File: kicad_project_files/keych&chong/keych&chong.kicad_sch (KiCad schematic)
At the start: 229 parts, among them J1 USB_C_Receptacle_USB2.0, U1 ATmega32U4-A, Y1 Crystal

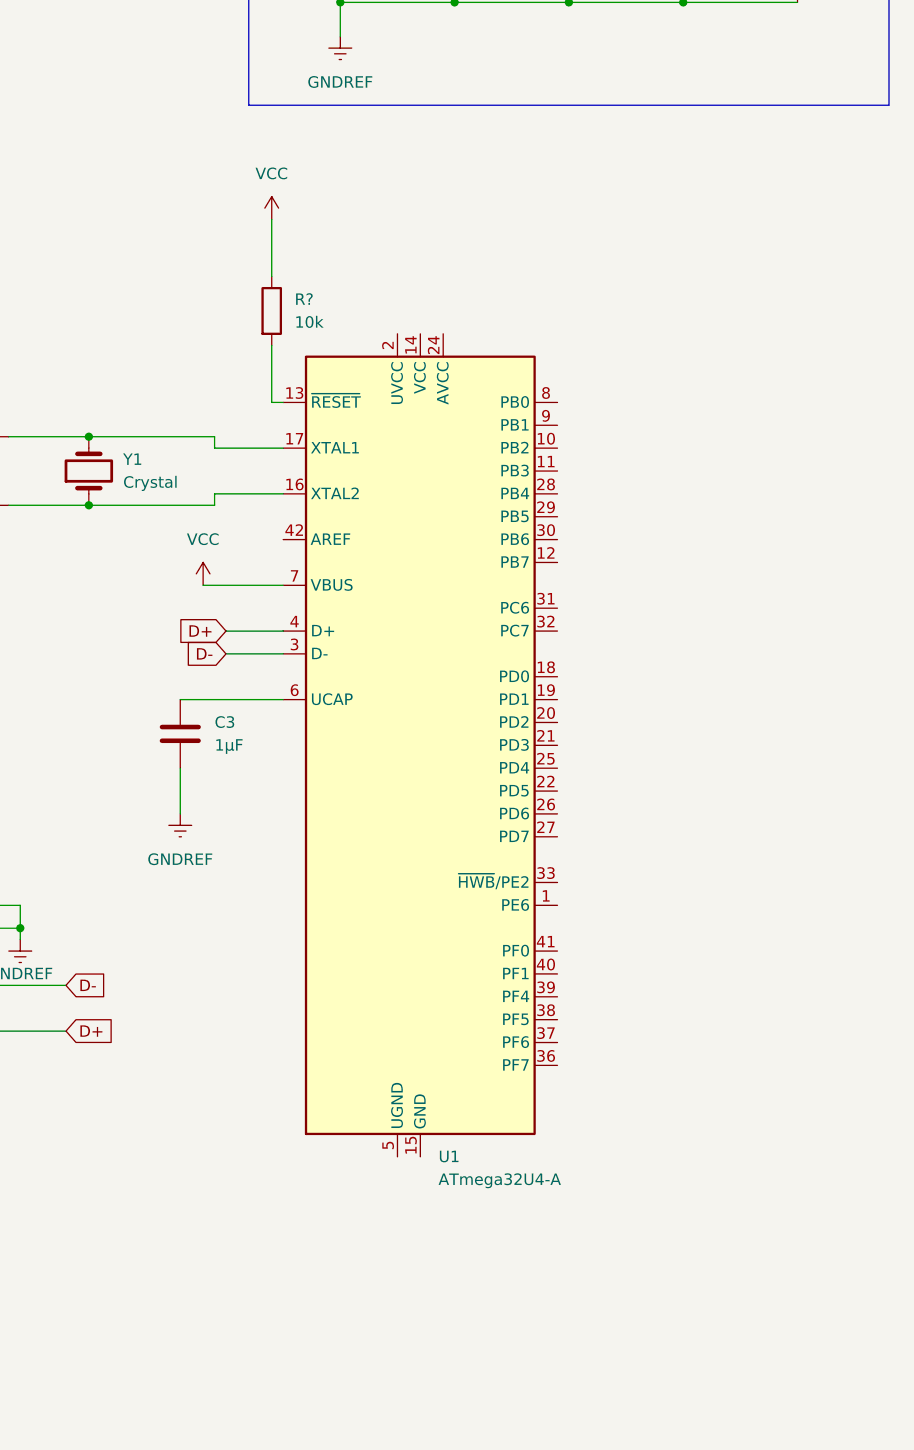
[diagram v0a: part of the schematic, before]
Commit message: refactor folder structure and add test circuit
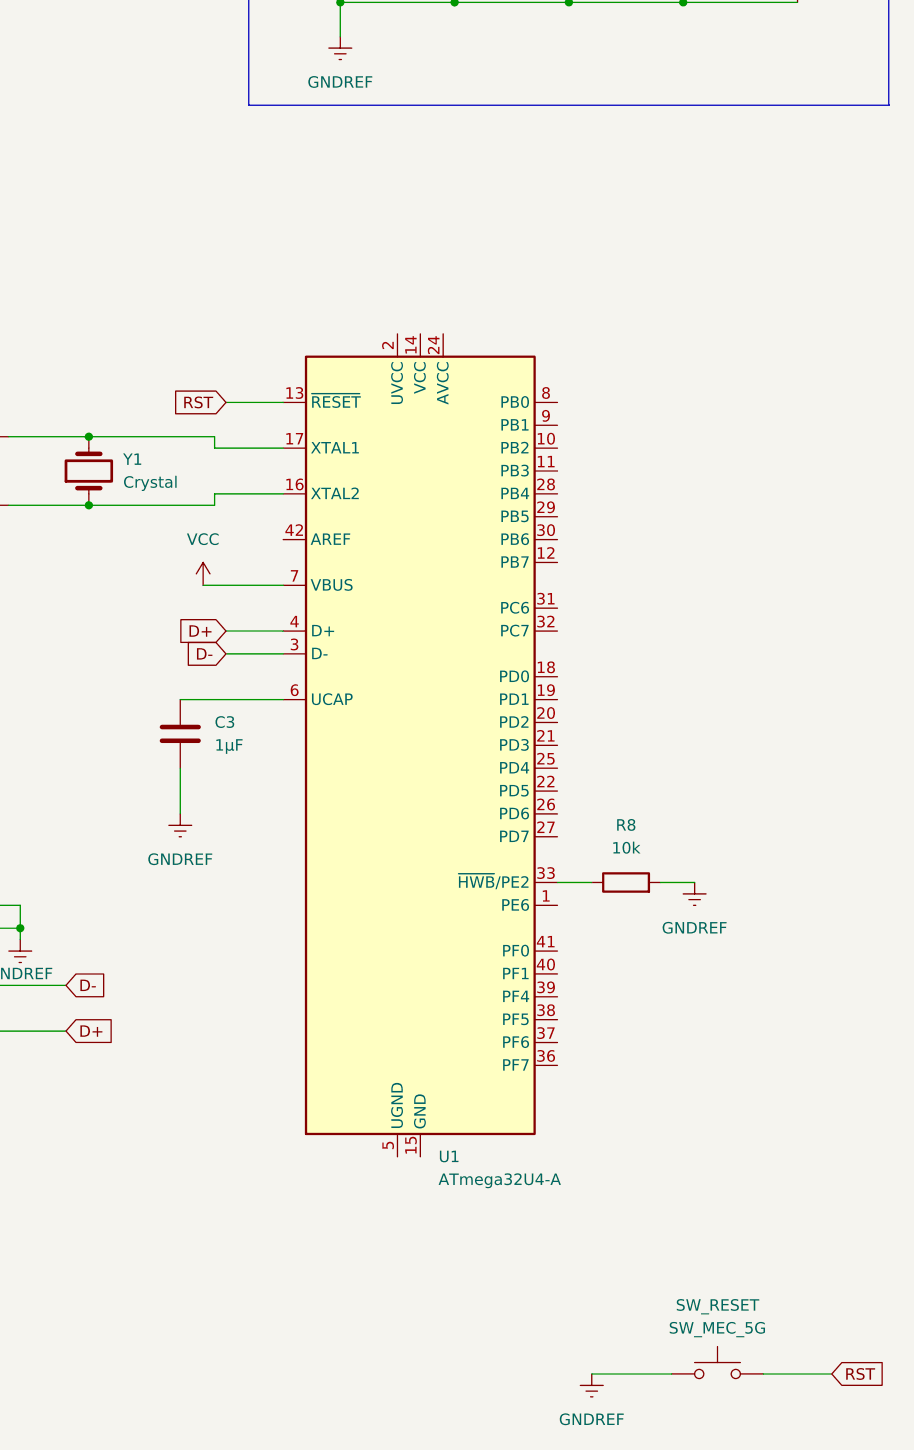
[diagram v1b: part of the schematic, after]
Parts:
- removed R?: 10k, symbol Device:R
- added R8: 10k, symbol Device:R
- added SW_RESET: SW_MEC_5G, symbol Switch:SW_MEC_5G
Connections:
- net GNDREF: now also R8.2, SW_RESET.1 (A), SW_RESET.2 (A)
- net RST: now reaches U1.13 (~{RESET})
- net RST: now also SW_RESET.3 (B), SW_RESET.4 (B)
- net at U1.33 (~{HWB}/PE2): now also R8.1
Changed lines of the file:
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@@
     (stroke (width 0) (type default) (color 0 0 0 0))
   )
-  (wire (pts (xy 326.39 132.08) (xy 326.39 125.73))
-    (stroke (width 0) (type default) (color 0 0 0 0))
-  )
   (wire (pts (xy 228.6 73.66) (xy 243.84 73.66))
     (stroke (width 0) (type default) (color 0 0 0 0))
@@
     (stroke (width 0) (type default) (color 0 0 0 0))
   )
+  (wire (pts (xy 381 240.03) (xy 388.62 240.03))
+    (stroke (width 0) (type default) (color 0 0 0 0))
+  )
   (wire (pts (xy 147.32 129.54) (xy 147.32 151.13))
     (stroke (width 0) (type default) (color 0 0 0 0))
@@
     (stroke (width 0) (type default) (color 0 0 0 0))
   )
+  (wire (pts (xy 369.57 185.42) (xy 373.38 185.42))
+    (stroke (width 0) (type default) (color 0 0 0 0))
+  )
   (wire (pts (xy 137.16 116.84) (xy 152.4 116.84))
     (stroke (width 0) (type default) (color 0 0 0 0))
@@
     (stroke (width 0) (type default) (color 0 0 0 0))
   )
-  (wire (pts (xy 327.66 132.08) (xy 326.39 132.08))
+  (wire (pts (xy 321.31 132.08) (xy 327.66 132.08))
     (stroke (width 0) (type default) (color 0 0 0 0))
   )
@@
     (stroke (width 0) (type default) (color 0 0 0 0))
   )
+  (wire (pts (xy 358.14 185.42) (xy 361.95 185.42))
+    (stroke (width 0) (type default) (color 0 0 0 0))
+  )
   (wire (pts (xy 106.68 106.68) (xy 106.68 109.22))
     (stroke (width 0) (type default) (color 0 0 0 0))
@@
     (stroke (width 0) (type default) (color 0 0 0 0))
   )
+  (wire (pts (xy 361.95 240.03) (xy 370.84 240.03))
+    (stroke (width 0) (type default) (color 0 0 0 0))
+  )
   (wire (pts (xy 76.2 161.29) (xy 91.44 161.29))
     (stroke (width 0) (type default) (color 0 0 0 0))
@@
     (stroke (width 0) (type default) (color 0 0 0 0))
   )
-  (wire (pts (xy 326.39 111.76) (xy 326.39 118.11))
-    (stroke (width 0) (type default) (color 0 0 0 0))
-  )
   (polyline (pts (xy 337.82 64.77) (xy 394.97 64.77))
     (stroke (width 0) (type default) (color 0 0 0 0))
@@
     )
   )
+  (global_label "RST" (shape input) (at 388.62 240.03 0) (fields_autoplaced)
+    (effects (font (size 1.27 1.27)) (justify left))
+    (property "Intersheet References" "${INTERSHEET_REFS}" (id 0) (at 394.4802 239.9506 0)
+      (effects (font (size 1.27 1.27)) (justify left) hide)
+    )
+  )
   (global_label "ROW_5" (shape input) (at 22.86 140.97 180) (fields_autoplaced)
     (effects (font (size 1.27 1.27)) (justify right))
@@
     )
   )
+  (global_label "RST" (shape input) (at 321.31 132.08 180) (fields_autoplaced)
+    (effects (font (size 1.27 1.27)) (justify right))
+    (property "Intersheet References" "${INTERSHEET_REFS}" (id 0) (at 315.4498 132.0006 0)
+      (effects (font (size 1.27 1.27)) (justify right) hide)
+    )
+  )
   (global_label "ROW_6" (shape input) (at 22.86 163.83 180) (fields_autoplaced)
     (effects (font (size 1.27 1.27)) (justify right))
@@
     (pin "4")
   )
+  (symbol (lib_id "Device:R") (at 365.76 185.42 90) (unit 1)
+    (in_bom yes) (on_board yes) (fields_autoplaced)
+    (property "Reference" "R8" (id 0) (at 365.76 179.07 90))
+    (property "Value" "10k" (id 1) (at 365.76 181.61 90))
+    (property "Footprint" "" (id 2) (at 365.76 187.198 90)
+      (effects (font (size 1.27 1.27)) hide)
+    )
+    (property "Datasheet" "~" (id 3) (at 365.76 185.42 0)
+      (effects (font (size 1.27 1.27)) hide)
+    )
+    (pin "1")
+    (pin "2")
+  )
   (symbol (lib_id "Switch:SW_MEC_5G") (at 264.16 41.91 0) (unit 1)
     (in_bom yes) (on_board yes) (fields_autoplaced)
@@
     (pin "4")
   )
-  (symbol (lib_id "power:VCC") (at 326.39 111.76 0) (unit 1)
-    (in_bom yes) (on_board yes) (fields_autoplaced)
-    (property "Reference" "#PWR?" (id 0) (at 326.39 115.57 0)
-      (effects (font (size 1.27 1.27)) hide)
-    )
-    (property "Value" "VCC" (id 1) (at 326.39 106.68 0))
-    (property "Footprint" "" (id 2) (at 326.39 111.76 0)
-      (effects (font (size 1.27 1.27)) hide)
-    )
-    (property "Datasheet" "" (id 3) (at 326.39 111.76 0)
-      (effects (font (size 1.27 1.27)) hide)
-    )
-    (pin "1")
-  )
   (symbol (lib_id "Diode:1N4148") (at 91.44 69.85 90) (unit 1)
     (in_bom yes) (on_board yes) (fields_autoplaced)
@@
     (pin "4")
   )
+  (symbol (lib_id "power:GNDREF") (at 373.38 185.42 0) (unit 1)
+    (in_bom yes) (on_board yes) (fields_autoplaced)
+    (property "Reference" "#PWR013" (id 0) (at 373.38 191.77 0)
+      (effects (font (size 1.27 1.27)) hide)
+    )
+    (property "Value" "GNDREF" (id 1) (at 373.38 190.5 0))
+    (property "Footprint" "" (id 2) (at 373.38 185.42 0)
+      (effects (font (size 1.27 1.27)) hide)
+    )
+    (property "Datasheet" "" (id 3) (at 373.38 185.42 0)
+      (effects (font (size 1.27 1.27)) hide)
+    )
+    (pin "1")
+  )
   (symbol (lib_id "power:VCC") (at 334.01 76.2 0) (unit 1)
     (in_bom yes) (on_board yes) (fields_autoplaced)
@@
     (pin "4")
   )
-  (symbol (lib_id "Device:R") (at 326.39 121.92 0) (unit 1)
-    (in_bom yes) (on_board yes) (fields_autoplaced)
-    (property "Reference" "R?" (id 0) (at 328.93 120.6499 0)
-      (effects (font (size 1.27 1.27)) (justify left))
-    )
-    (property "Value" "10k" (id 1) (at 328.93 123.1899 0)
-      (effects (font (size 1.27 1.27)) (justify left))
-    )
-    (property "Footprint" "" (id 2) (at 324.612 121.92 90)
-      (effects (font (size 1.27 1.27)) hide)
-    )
-    (property "Datasheet" "~" (id 3) (at 326.39 121.92 0)
-      (effects (font (size 1.27 1.27)) hide)
-    )
-    (pin "1")
-    (pin "2")
-  )
   (symbol (lib_id "Diode:1N4148") (at 152.4 69.85 90) (unit 1)
     (in_bom yes) (on_board yes) (fields_autoplaced)
@@
     (pin "4")
   )
+  (symbol (lib_id "power:GNDREF") (at 361.95 240.03 0) (unit 1)
+    (in_bom yes) (on_board yes) (fields_autoplaced)
+    (property "Reference" "#PWR012" (id 0) (at 361.95 246.38 0)
+      (effects (font (size 1.27 1.27)) hide)
+    )
+    (property "Value" "GNDREF" (id 1) (at 361.95 245.11 0))
+    (property "Footprint" "" (id 2) (at 361.95 240.03 0)
+      (effects (font (size 1.27 1.27)) hide)
+    )
+    (property "Datasheet" "" (id 3) (at 361.95 240.03 0)
+      (effects (font (size 1.27 1.27)) hide)
+    )
+    (pin "1")
+  )
   (symbol (lib_id "Diode:1N4148") (at 45.72 157.48 90) (unit 1)
     (in_bom yes) (on_board yes) (fields_autoplaced)
@@
     (pin "2")
   )
+  (symbol (lib_id "Switch:SW_MEC_5G") (at 375.92 240.03 0) (unit 1)
+    (in_bom yes) (on_board yes) (fields_autoplaced)
+    (property "Reference" "SW_RESET" (id 0) (at 375.92 232.41 0))
+    (property "Value" "SW_MEC_5G" (id 1) (at 375.92 234.95 0))
+    (property "Footprint" "" (id 2) (at 375.92 234.95 0)
+      (effects (font (size 1.27 1.27)) hide)
+    )
+    (property "Datasheet" "http://www.apem.com/int/index.php?controller=attachment&id_attachment=488" (id 3) (at 375.92 234.95 0)
+      (effects (font (size 1.27 1.27)) hide)
+    )
+    (pin "1")
+    (pin "3")
+    (pin "2")
+    (pin "4")
+  )
   (symbol (lib_id "Diode:1N4148") (at 45.72 113.03 90) (unit 1)
     (in_bom yes) (on_board yes) (fields_autoplaced)
@@
       (reference "#PWR011") (unit 1) (value "VCC") (footprint "")
     )
-    (path "/570266db-1a9a-4c3f-971a-1124e4078345"
-      (reference "#PWR?") (unit 1) (value "VCC") (footprint "")
+    (path "/d9ab6604-7028-4c35-8e6f-0aab5fc7c5be"
+      (reference "#PWR012") (unit 1) (value "GNDREF") (footprint "")
+    )
+    (path "/8469fb4b-027f-422e-a9b3-52e1f29db5cc"
+      (reference "#PWR013") (unit 1) (value "GNDREF") (footprint "")
     )
     (path "/a98f613d-600e-4d8b-958d-afe5883a7f6c"
@@
       (reference "R7") (unit 1) (value "22ohm") (footprint "")
     )
-    (path "/b9643a31-044f-4836-ab1f-132b5bd3619e"
-      (reference "R?") (unit 1) (value "10k") (footprint "")
+    (path "/4b36f467-2d4e-43cf-9ce6-750edb207425"
+      (reference "R8") (unit 1) (value "10k") (footprint "")
     )
     (path "/74e04d55-3406-412a-8d4d-73659f0bd63a"
@@
       (reference "SW_R1") (unit 1) (value "SW_MEC_5G") (footprint "")
     )
+    (path "/f73d5f45-bf04-4553-a792-1e4a94053fa4"
+      (reference "SW_RESET") (unit 1) (value "SW_MEC_5G") (footprint "")
+    )
     (path "/2620d00d-6d7b-419d-b4a7-686a0b95ded7"

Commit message: connect schematic
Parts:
- added ISCP: Conn_02x03_Odd_Even, symbol Connector_Generic:Conn_02x03_Odd_Even
- added R?: 10k, symbol Device:R
- C7: value 10µF -> 1µF
- R1, R2: value R -> 220ohm
- Y1: value Crystal -> 16mhz
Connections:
- net CAPS: now also U1.37 (PF6)
- net COL_1: now also SW_F12.3 (B), SW_F12.4 (B), U1.8 (PB0)
- net COL_10: now also U1.32 (PC7)
- net COL_11: now also U1.18 (PD0)
- net COL_12: now also U1.19 (PD1)
- net COL_13: now also U1.20 (PD2)
- net COL_14: now also U1.21 (PD3)
- net COL_15: now also U1.25 (PD4)
- net COL_16: now also U1.22 (PD5)
- net COL_2: now also SW_PSE-BK1.3 (B), SW_PSE-BK1.4 (B), U1.9 (PB1), ISCP.1 (Pin_1)
- net COL_3: now also SW_NUM-ASTR1.3 (B), SW_NUM-ASTR1.4 (B), U1.10 (PB2), ISCP.3 (Pin_3)
- net COL_4: now also SW_NUM-MINUS1.3 (B), SW_NUM-MINUS1.4 (B), U1.11 (PB3), ISCP.5 (Pin_5)
- net COL_5: now also SW_NUM-PLUS1.3 (B), SW_NUM-PLUS1.4 (B), U1.28 (PB4)
- net COL_6: now also SW_PG-UP1.3 (B), SW_PG-UP1.4 (B), U1.29 (PB5)
- net COL_7: now also SW_PG-DN1.3 (B), SW_PG-DN1.4 (B), U1.30 (PB6)
- net COL_8: now also SW_NUM-LK1.3 (B), SW_NUM-LK1.4 (B), U1.12 (PB7)
- net COL_9: now also U1.31 (PC6)
- net GNDREF: now also U1.15 (GND), U1.23 (GND), U1.35 (GND), U1.43 (GND), U1.5 (UGND), ISCP.6 (Pin_6)
- net NUM: now also U1.36 (PF7)
- net ROW_1: now also U1.26 (PD6)
- net ROW_2: now also U1.27 (PD7)
- net ROW_3: now also U1.1 (PE6)
- net ROW_4: now also U1.41 (PF0)
- net ROW_5: now also U1.40 (PF1)
- net ROW_6: now also U1.39 (PF4)
- net ROW_7: now also D100.1 (K), D101.1 (K), D102.1 (K), D103.1 (K), D104.1 (K), D97.1 (K), D98.1 (K), D99.1 (K), U1.38 (PF5)
- net RST: now also R?.1
- net VCC: now also U1.14 (VCC), U1.2 (UVCC), U1.24 (AVCC), U1.34 (VCC), U1.44 (AVCC), ISCP.2 (Pin_2), R?.2
- new net RESET: ISCP.4 (Pin_4)
- no-connect marks 2 -> 3
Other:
- moved on the sheet: C1, C2, C3, D102, D103, D104, J1, R3, R4, R5, R6, R7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

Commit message: add diode to usb input voltage
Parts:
- added D?: 1N4148, Diode_THT:D_DO-35_SOD27_P7.62mm_Horizontal, symbol Diode:1N4148
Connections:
- net VCC: now also D?.1 (K); no longer J1.A4 (VBUS), J1.A9 (VBUS), J1.B4 (VBUS), J1.B9 (VBUS)
- new net: D?.2 (A), J1.A4 (VBUS), J1.A9 (VBUS), J1.B4 (VBUS), J1.B9 (VBUS)
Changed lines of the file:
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@@
   (junction (at 55.88 129.54) (diameter 0) (color 0 0 0 0)
   )
-  (junction (at 372.11 173.99) (diameter 0) (color 0 0 0 0)
-  )
   (junction (at 167.64 52.07) (diameter 0) (color 0 0 0 0)
   )
@@
   (junction (at 76.2 139.7) (diameter 0) (color 0 0 0 0)
   )
+  (junction (at 378.46 173.99) (diameter 0) (color 0 0 0 0)
+  )
   (junction (at 55.88 63.5) (diameter 0) (color 0 0 0 0)
   )
@@
     (stroke (width 0) (type default) (color 0 0 0 0))
   )
-  (wire (pts (xy 372.11 173.99) (xy 377.19 173.99))
+  (wire (pts (xy 378.46 173.99) (xy 383.54 173.99))
     (stroke (width 0) (type default) (color 0 0 0 0))
   )
@@
     (stroke (width 0) (type default) (color 0 0 0 0))
   )
-  (wire (pts (xy 370.84 173.99) (xy 372.11 173.99))
-    (stroke (width 0) (type default) (color 0 0 0 0))
-  )
   (wire (pts (xy 137.16 139.7) (xy 152.4 139.7))
     (stroke (width 0) (type default) (color 0 0 0 0))
@@
     (stroke (width 0) (type default) (color 0 0 0 0))
   )
-  (wire (pts (xy 372.11 167.64) (xy 372.11 173.99))
+  (wire (pts (xy 378.46 167.64) (xy 378.46 173.99))
     (stroke (width 0) (type default) (color 0 0 0 0))
   )
@@
     (pin "4")
   )
-  (symbol (lib_id "power:PWR_FLAG") (at 372.11 167.64 0) (unit 1)
+  (symbol (lib_id "power:PWR_FLAG") (at 378.46 167.64 0) (unit 1)
     (in_bom yes) (on_board yes) (fields_autoplaced)
-    (property "Reference" "#FLG?" (id 0) (at 372.11 165.735 0)
+    (property "Reference" "#FLG?" (id 0) (at 378.46 165.735 0)
       (effects (font (size 1.27 1.27)) hide)
     )
-    (property "Value" "PWR_FLAG" (id 1) (at 372.11 162.56 0))
-    (property "Footprint" "" (id 2) (at 372.11 167.64 0)
+    (property "Value" "PWR_FLAG" (id 1) (at 378.46 162.56 0))
+    (property "Footprint" "" (id 2) (at 378.46 167.64 0)
       (effects (font (size 1.27 1.27)) hide)
     )
-    (property "Datasheet" "~" (id 3) (at 372.11 167.64 0)
+    (property "Datasheet" "~" (id 3) (at 378.46 167.64 0)
       (effects (font (size 1.27 1.27)) hide)
     )
@@
     (pin "2")
   )
+  (symbol (lib_id "Diode:1N4148") (at 374.65 173.99 180) (unit 1)
+    (in_bom yes) (on_board yes) (fields_autoplaced)
+    (property "Reference" "D?" (id 0) (at 374.65 167.64 0))
+    (property "Value" "1N4148" (id 1) (at 374.65 170.18 0))
+    (property "Footprint" "Diode_THT:D_DO-35_SOD27_P7.62mm_Horizontal" (id 2) (at 374.65 169.545 0)
+      (effects (font (size 1.27 1.27)) hide)
+    )
+    (property "Datasheet" "https://assets.nexperia.com/documents/data-sheet/1N4148_1N4448.pdf" (id 3) (at 374.65 173.99 0)
+      (effects (font (size 1.27 1.27)) hide)
+    )
+    (pin "1")
+    (pin "2")
+  )
   (symbol (lib_id "Diode:1N4148") (at 213.36 157.48 90) (unit 1)
     (in_bom yes) (on_board yes) (fields_autoplaced)
@@
     (pin "4")
   )
-  (symbol (lib_id "power:VCC") (at 377.19 173.99 0) (unit 1)
+  (symbol (lib_id "power:VCC") (at 383.54 173.99 0) (unit 1)
     (in_bom yes) (on_board yes) (fields_autoplaced)
-    (property "Reference" "#PWR09" (id 0) (at 377.19 177.8 0)
+    (property "Reference" "#PWR09" (id 0) (at 383.54 177.8 0)
       (effects (font (size 1.27 1.27)) hide)
     )
-    (property "Value" "VCC" (id 1) (at 377.19 168.91 0))
-    (property "Footprint" "" (id 2) (at 377.19 173.99 0)
+    (property "Value" "VCC" (id 1) (at 383.54 168.91 0))
+    (property "Footprint" "" (id 2) (at 383.54 173.99 0)
       (effects (font (size 1.27 1.27)) hide)
     )
-    (property "Datasheet" "" (id 3) (at 377.19 173.99 0)
+    (property "Datasheet" "" (id 3) (at 383.54 173.99 0)
       (effects (font (size 1.27 1.27)) hide)
     )
@@
       (reference "D106") (unit 1) (value "LED") (footprint "")
     )
+    (path "/1767b76a-d6ac-48b3-a8f6-ed12f684902a"
+      (reference "D?") (unit 1) (value "1N4148") (footprint "Diode_THT:D_DO-35_SOD27_P7.62mm_Horizontal")
+    )
     (path "/fab12cff-f0ef-4023-9d9a-1274eae4f0d8"
